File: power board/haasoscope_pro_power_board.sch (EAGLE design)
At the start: 94 parts, among them IC1 TPS5430DDAR, IC10 TPS5430DDAR, IC12 TPS7A7200RGTR, IC2 TPS5430DDAR, IC3 TPS7A7200RGTR, IC4 TPS5430DDAR, IC5 TPS72325DBVR, IC6 TPS5430DDAR, IC7 TPS7A7200RGTR, IC8 TPS5430DDAR, IC9 TPS7A7200RGTR, J1 2p-2.54, J10 2p-2.54, J11 2p-2.54, J13 2p-2.54, J2 2p-2.54, J3 2p-2.54, J4 2p-2.54, J5 2p-2.54, J6 2p-2.54, J7 2p-2.54, J8 2p-2.54, J9 2p-2.54

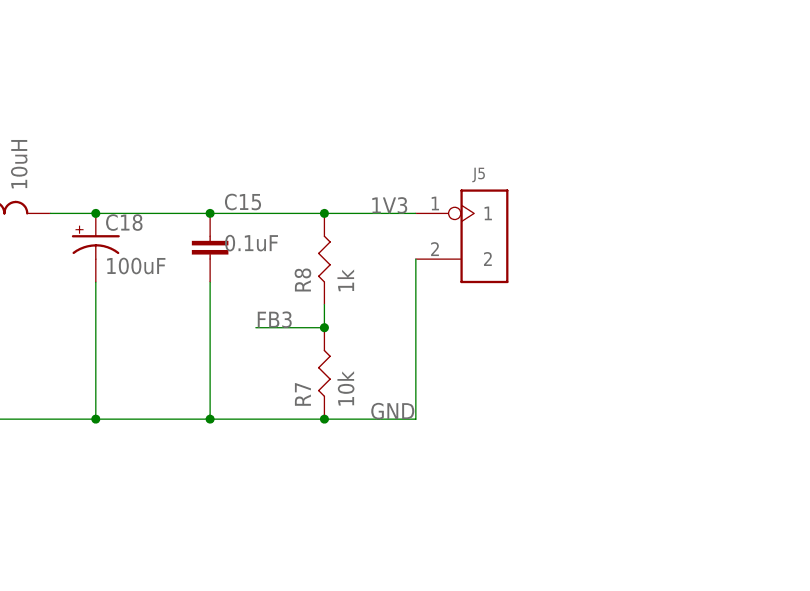
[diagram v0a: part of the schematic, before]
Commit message: 1.3->1.8 V for VLVDS
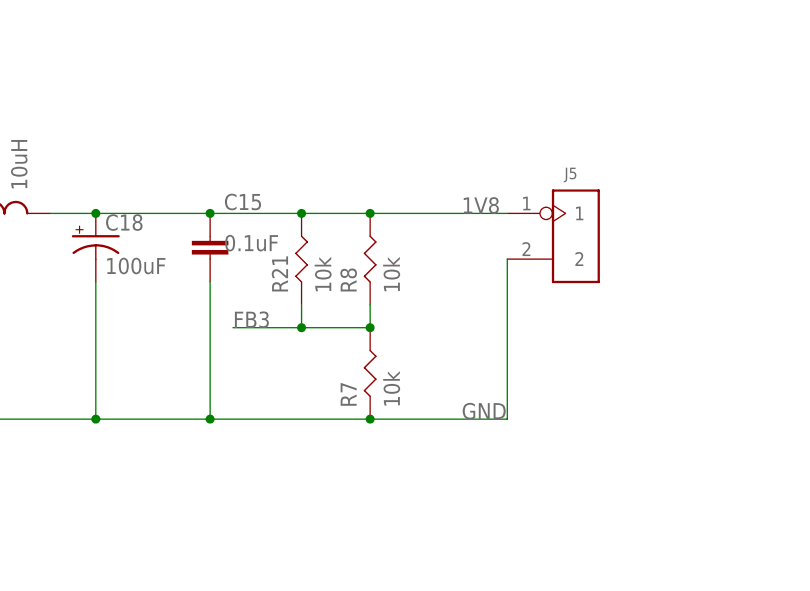
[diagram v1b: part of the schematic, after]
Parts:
- added R21: 10k, FlashPCB_Resistors:RES-0402
- R8: value 1k -> 10k
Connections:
- removed net 1V3: C15.1, C18.+, J5.1, L4.2, R8.P$2
- new net 1V8: C15.1, C18.+, J5.1, L4.2, R21.P$2, R8.P$2
- net FB3: now also R21.P$1
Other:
- note added: "VLVDS ~ 1.8V"
- note added: "Vout = (5k/10k +1) * 1.221 V =1.5*1.221 V = ~ 1.8V"
- note removed: "VLVDS ~ 1.3V"
- note removed: "Vout = (R8/R7 +1) * 1.221 V =1.1*1.221 V = ~ 1.3V"
- moved on the sheet: J5, R7, R8
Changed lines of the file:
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@@
 </part>
 <part name="IC4" library="TPS5430DDAR" deviceset="TPS5430DDAR" device=""/>
-<part name="R8" library="FlashPCB_Resistors" deviceset="RES-0402" device="" value="1k"/>
+<part name="R8" library="FlashPCB_Resistors" deviceset="RES-0402" device="" value="10k"/>
 <part name="L6" library="SparkFun-Passives" deviceset="INDUCTOR" device="PWR" value="10uH">
 <attribute name="LCSC" value="C339970"/>
@@
 <part name="R18" library="FlashPCB_Resistors" deviceset="RES-0402" device="" value="3.3k"/>
 <part name="GND15" library="SparkFun-PowerSymbols" library_urn="urn:adsk.eagle:library:530" deviceset="GND" device=""/>
+<part name="R21" library="FlashPCB_Resistors" deviceset="RES-0402" device="" value="10k"/>
 </parts>
 <sheets>
@@
 <text x="149.86" y="17.78" size="1.778" layer="90">Vout = -(Rtop/Rbot +1) * 1.221 V
 = -2.33*1.221 V = ~ -2.8V</text>
-<text x="137.16" y="124.46" size="1.778" layer="90">Vout = (R8/R7 +1) * 1.221 V
-=1.1*1.221 V = ~ 1.3V</text>
+<text x="137.16" y="124.46" size="1.778" layer="90">Vout = (5k/10k +1) * 1.221 V
+=1.5*1.221 V = ~ 1.8V</text>
 <text x="137.16" y="187.96" size="1.778" layer="90">Vout = (R12/R11 +1) * 1.221 V
 =2*1.221 V = ~ 2.4V</text>
@@
 <text x="137.16" y="325.12" size="1.778" layer="90">Vout = (R20/R19 +1) * 1.221 V
 =3*1.221 V = ~ 3.7V</text>
-<text x="177.8" y="109.22" size="1.778" layer="90">VLVDS ~ 1.3V</text>
+<text x="187.96" y="109.22" size="1.778" layer="90">VLVDS ~ 1.8V</text>
 <text x="177.8" y="48.26" size="1.778" layer="90">V+ for input amp reg ~ 2.8V</text>
 <text x="177.8" y="-5.08" size="1.778" layer="90">V- for input amp reg ~ -2.8V</text>
@@
 <attribute name="LCSC" x="124.46" y="121.92" size="1.778" layer="96" rot="R90" display="off"/>
 </instance>
-<instance part="R7" gate="G$1" x="162.56" y="104.14" smashed="yes" rot="R90">
-<attribute name="NAME" x="161.0614" y="100.33" size="1.778" layer="95" rot="R90"/>
-<attribute name="VALUE" x="165.862" y="100.33" size="1.778" layer="96" rot="R90"/>
+<instance part="R7" gate="G$1" x="167.64" y="104.14" smashed="yes" rot="R90">
+<attribute name="NAME" x="166.1414" y="100.33" size="1.778" layer="95" rot="R90"/>
+<attribute name="VALUE" x="170.942" y="100.33" size="1.778" layer="96" rot="R90"/>
 </instance>
 <instance part="D4" gate="G$1" x="109.22" y="114.3" smashed="yes" rot="R90">
@@
 <attribute name="LCSC" x="109.22" y="114.3" size="1.778" layer="96" rot="R90" display="off"/>
 </instance>
-<instance part="J5" gate="G$1" x="180.34" y="119.38" smashed="yes">
-<attribute name="NAME" x="179.07" y="125.73" size="1.27" layer="95" ratio="10"/>
+<instance part="J5" gate="G$1" x="190.5" y="119.38" smashed="yes">
+<attribute name="NAME" x="189.23" y="125.73" size="1.27" layer="95" ratio="10"/>
 </instance>
 <instance part="C15" gate="C$1" x="149.86" y="119.38" smashed="yes">
@@
 <attribute name="VALUE" x="16.51" y="127" size="1.778" layer="96" align="center-left"/>
 </instance>
-<instance part="R8" gate="G$1" x="162.56" y="116.84" smashed="yes" rot="R90">
-<attribute name="NAME" x="161.0614" y="113.03" size="1.778" layer="95" rot="R90"/>
-<attribute name="VALUE" x="165.862" y="113.03" size="1.778" layer="96" rot="R90"/>
+<instance part="R8" gate="G$1" x="167.64" y="116.84" smashed="yes" rot="R90">
+<attribute name="NAME" x="166.1414" y="113.03" size="1.778" layer="95" rot="R90"/>
+<attribute name="VALUE" x="170.942" y="113.03" size="1.778" layer="96" rot="R90"/>
 </instance>
 <instance part="L6" gate="G$1" x="124.46" y="185.42" smashed="yes" rot="R90">
@@
 <instance part="GND15" gate="1" x="314.96" y="345.44" smashed="yes">
 <attribute name="VALUE" x="314.96" y="345.186" size="1.778" layer="96" align="top-center"/>
+</instance>
+<instance part="R21" gate="G$1" x="160.02" y="116.84" smashed="yes" rot="R90">
+<attribute name="NAME" x="158.5214" y="113.03" size="1.778" layer="95" rot="R90"/>
+<attribute name="VALUE" x="163.322" y="113.03" size="1.778" layer="96" rot="R90"/>
 </instance>
 </instances>
@@
 <segment>
 <pinref part="R7" gate="G$1" pin="P$1"/>
-<wire x1="172.72" y1="99.06" x2="162.56" y2="99.06" width="0.1524" layer="91"/>
+<wire x1="182.88" y1="99.06" x2="167.64" y2="99.06" width="0.1524" layer="91"/>
 <pinref part="D4" gate="G$1" pin="A"/>
 <wire x1="109.22" y1="111.76" x2="109.22" y2="99.06" width="0.1524" layer="91"/>
 <wire x1="109.22" y1="99.06" x2="137.16" y2="99.06" width="0.1524" layer="91"/>
-<junction x="162.56" y="99.06"/>
+<junction x="167.64" y="99.06"/>
 <wire x1="137.16" y1="99.06" x2="149.86" y2="99.06" width="0.1524" layer="91"/>
-<wire x1="149.86" y1="99.06" x2="162.56" y2="99.06" width="0.1524" layer="91"/>
+<wire x1="149.86" y1="99.06" x2="167.64" y2="99.06" width="0.1524" layer="91"/>
 <wire x1="137.16" y1="114.3" x2="137.16" y2="99.06" width="0.1524" layer="91"/>
 <junction x="137.16" y="99.06"/>
 <wire x1="149.86" y1="114.3" x2="149.86" y2="99.06" width="0.1524" layer="91"/>
 <junction x="149.86" y="99.06"/>
-<label x="167.64" y="99.06" size="1.778" layer="95"/>
+<label x="177.8" y="99.06" size="1.778" layer="95"/>
 <pinref part="J5" gate="G$1" pin="2"/>
-<wire x1="172.72" y1="116.84" x2="172.72" y2="99.06" width="0.1524" layer="91"/>
+<wire x1="182.88" y1="116.84" x2="182.88" y2="99.06" width="0.1524" layer="91"/>
 <pinref part="C15" gate="C$1" pin="2"/>
 <pinref part="C18" gate="G$1" pin="-"/>
@@
 </segment>
 <segment>
-<label x="154.94" y="109.22" size="1.778" layer="95"/>
+<label x="152.4" y="109.22" size="1.778" layer="95"/>
 <pinref part="R7" gate="G$1" pin="P$2"/>
-<wire x1="154.94" y1="109.22" x2="162.56" y2="109.22" width="0.1524" layer="91"/>
-<wire x1="162.56" y1="111.76" x2="162.56" y2="109.22" width="0.1524" layer="91"/>
-<junction x="162.56" y="109.22"/>
+<wire x1="152.4" y1="109.22" x2="160.02" y2="109.22" width="0.1524" layer="91"/>
+<wire x1="160.02" y1="109.22" x2="167.64" y2="109.22" width="0.1524" layer="91"/>
+<wire x1="167.64" y1="111.76" x2="167.64" y2="109.22" width="0.1524" layer="91"/>
+<junction x="167.64" y="109.22"/>
 <pinref part="R8" gate="G$1" pin="P$1"/>
-</segment>
-</net>
-<net name="1V3" class="0">
+<pinref part="R21" gate="G$1" pin="P$1"/>
+<wire x1="160.02" y1="111.76" x2="160.02" y2="109.22" width="0.1524" layer="91"/>
+<junction x="160.02" y="109.22"/>
+</segment>
+</net>
+<net name="1V8" class="0">
 <segment>
 <pinref part="L4" gate="G$1" pin="2"/>
 <wire x1="132.08" y1="121.92" x2="137.16" y2="121.92" width="0.1524" layer="91"/>
 <wire x1="137.16" y1="121.92" x2="149.86" y2="121.92" width="0.1524" layer="91"/>
-<wire x1="149.86" y1="121.92" x2="162.56" y2="121.92" width="0.1524" layer="91"/>
-<label x="167.64" y="121.92" size="1.778" layer="95"/>
+<wire x1="149.86" y1="121.92" x2="160.02" y2="121.92" width="0.1524" layer="91"/>
+<label x="177.8" y="121.92" size="1.778" layer="95"/>
 <pinref part="J5" gate="G$1" pin="1"/>
 <pinref part="C15" gate="C$1" pin="1"/>
@@
 <pinref part="C18" gate="G$1" pin="+"/>
 <junction x="137.16" y="121.92"/>
-<wire x1="162.56" y1="121.92" x2="172.72" y2="121.92" width="0.1524" layer="91"/>
+<wire x1="160.02" y1="121.92" x2="167.64" y2="121.92" width="0.1524" layer="91"/>
+<wire x1="167.64" y1="121.92" x2="182.88" y2="121.92" width="0.1524" layer="91"/>
 <pinref part="R8" gate="G$1" pin="P$2"/>
-<junction x="162.56" y="121.92"/>
-</segment>
-</net>
+<junction x="167.64" y="121.92"/>
+<pinref part="R21" gate="G$1" pin="P$2"/>
+<junction x="160.02" y="121.92"/>
+</segment>
+</net>

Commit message: add 2.5D for fpga, and add 1V9D for VLVDS
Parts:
- added C28, C38: 10uF, Nordic_nRF:CAPACITOR_0805_N
- added C29, C43: 0.1uF, Nordic_nRF:CAPACITOR_0402_N
- added IC11, IC14: TPS7A7200RGTR, TPS7A7200RGTR:TPS7A7200RGTR
- added J12, J15: 2p-2.54, Seeed-Connector:DIP-BLACK-MALE-HEADER-VERT(2P-2.54)
- added R22, R24: 20k, FlashPCB_Resistors:RES-0402
- R8: value 10k -> 3.3k
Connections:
- removed net 1V8: C15.1, C18.+, J5.1, L4.2, R21.P$2, R8.P$2
- new net 1V9DOUT: C28.1, C29.1, IC11.OUT_1, IC11.OUT_2, IC11.SNS, J12.2, R22.P$1
- new net 2V5DOUT: C38.1, C43.1, IC14.OUT_1, IC14.OUT_2, IC14.SNS, J15.2, R24.P$1
- new net 2V8D: C15.1, C18.+, IC14.EN, IC14.IN_1, IC14.IN_2, J5.1, L4.2, R8.P$2
- new net N$7: R21.P$2, R8.P$1
- new net PG1V9D: IC11.PG, R22.P$2
- new net PG2V5D: IC14.PG, R24.P$2
- net 2V4: now also IC11.EN, IC11.IN_1, IC11.IN_2
- net FB3: no longer R8.P$1
- net GND: now also C28.2, C29.2, C38.2, C43.2, IC11.200MV, IC11.400MV, IC11.800MV, IC11.EP, IC11.GND, IC14.1.6V, IC14.400MV, IC14.800MV, IC14.EP, IC14.GND, J12.1, J15.1
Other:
- note added: "V+ for 2v5D reg ~ 2.8V"
- note added: "VLVDS = 1.9V"
- note removed: "VLVDS ~ 1.8V"
- note removed: "Vout = (5k/10k +1) * 1.221 V =1.5*1.221 V = ~ 1.8V"
- moved on the sheet: C1, C10, C13, C14, C2, C27, C3, C30, C35, C4, C5, C6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

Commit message: power connector etc
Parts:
- added J14: 8pin, SparkFun-Connectors:CONN_08"
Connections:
- net 1V1OUT: now also J14.4
- net 1V9DOUT: now also J14.6
- net 1V9OUT: now also J14.5
- net 2V5DOUT: now also J14.8
- net 3V3OUT: now also J14.1
- net GND: now also J14.2, J14.3, J14.7
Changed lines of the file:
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@@
 <part name="C43" library="Nordic_nRF" library_urn="urn:adsk.eagle:library:169009" deviceset="CAPACITOR" device="_0402_N" package3d_urn="urn:adsk.eagle:package:2593732/1" value="0.1uF"/>
 <part name="GND17" library="SparkFun-PowerSymbols" library_urn="urn:adsk.eagle:library:530" deviceset="GND" device=""/>
+<part name="J14" library="SparkFun-Connectors" library_urn="urn:adsk.eagle:library:513" deviceset="CONN_08" device="&quot;" package3d_urn="urn:adsk.eagle:package:38138/1" value="8pin"/>
 </parts>
 <sheets>
@@
 <attribute name="VALUE" x="279.4" y="129.286" size="1.778" layer="96" align="top-center"/>
 </instance>
+<instance part="J14" gate="G$1" x="365.76" y="2.54" smashed="yes" rot="R180"/>
 </instances>
 <busses>
@@
 <junction x="264.16" y="81.28"/>
 </segment>
+<segment>
+<wire x1="360.68" y1="7.62" x2="353.06" y2="7.62" width="0.1524" layer="91"/>
+<pinref part="J14" gate="G$1" pin="2"/>
+<label x="353.06" y="7.62" size="1.778" layer="95"/>
+</segment>
+<segment>
+<pinref part="J14" gate="G$1" pin="7"/>
+<wire x1="360.68" y1="-5.08" x2="353.06" y2="-5.08" width="0.1524" layer="91"/>
+<label x="353.06" y="-5.08" size="1.778" layer="95"/>
+</segment>
+<segment>
+<wire x1="360.68" y1="5.08" x2="353.06" y2="5.08" width="0.1524" layer="91"/>
+<pinref part="J14" gate="G$1" pin="3"/>
+<label x="353.06" y="5.08" size="1.778" layer="95"/>
+</segment>
 </net>
 <net name="SW1" class="0">
@@
 <label x="236.22" y="317.5" size="1.778" layer="95"/>
 </segment>
+<segment>
+<wire x1="360.68" y1="10.16" x2="353.06" y2="10.16" width="0.1524" layer="91"/>
+<label x="353.06" y="10.16" size="1.778" layer="95"/>
+<pinref part="J14" gate="G$1" pin="1"/>
+</segment>
 </net>
 <net name="PG3V3" class="0">
@@
 <label x="236.22" y="180.34" size="1.778" layer="95"/>
 </segment>
+<segment>
+<pinref part="J14" gate="G$1" pin="5"/>
+<wire x1="360.68" y1="0" x2="353.06" y2="0" width="0.1524" layer="91"/>
+<label x="350.52" y="0" size="1.778" layer="95"/>
+</segment>
 </net>
 <net name="PG1V9" class="0">
@@
 <label x="236.22" y="248.92" size="1.778" layer="95"/>
 </segment>
+<segment>
+<pinref part="J14" gate="G$1" pin="4"/>
+<wire x1="360.68" y1="2.54" x2="353.06" y2="2.54" width="0.1524" layer="91"/>
+<label x="350.52" y="2.54" size="1.778" layer="95"/>
+</segment>
 </net>
 <net name="PG1V1" class="0">
@@
 <junction x="365.76" y="213.36"/>
 </segment>
+<segment>
+<pinref part="J14" gate="G$1" pin="6"/>
+<wire x1="360.68" y1="-2.54" x2="353.06" y2="-2.54" width="0.1524" layer="91"/>
+<label x="350.52" y="-2.54" size="1.778" layer="95"/>
+</segment>
 </net>
 <net name="N$7" class="0">
@@
 <label x="236.22" y="106.68" size="1.778" layer="95"/>
 </segment>
-</net>
+<segment>
+<pinref part="J14" gate="G$1" pin="8"/>
+<wire x1="360.68" y1="-7.62" x2="353.06" y2="-7.62" width="0.1524" layer="91"/>
+<label x="353.06" y="-7.62" size="1.778" layer="95"/>
+</segment>
+</net>

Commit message: power connector etc
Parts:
- renumbered J14 to J16
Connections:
- net 1V1OUT: now also J16.2; no longer J16.4
- net 1V9DOUT: now also J16.4; no longer J16.6
- net 1V9OUT: now also J16.3; no longer J16.5
- net 2V5-: now also J16.8
- net 2V5DOUT: now also J16.6; no longer J16.8
- net 2V5OUT: now also J16.7
- net GND: now also J16.5; no longer J16.2, J16.3, J16.7
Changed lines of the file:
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@@
 <part name="C43" library="Nordic_nRF" library_urn="urn:adsk.eagle:library:169009" deviceset="CAPACITOR" device="_0402_N" package3d_urn="urn:adsk.eagle:package:2593732/1" value="0.1uF"/>
 <part name="GND17" library="SparkFun-PowerSymbols" library_urn="urn:adsk.eagle:library:530" deviceset="GND" device=""/>
-<part name="J14" library="SparkFun-Connectors" library_urn="urn:adsk.eagle:library:513" deviceset="CONN_08" device="&quot;" package3d_urn="urn:adsk.eagle:package:38138/1" value="8pin"/>
+<part name="J16" library="SparkFun-Connectors" library_urn="urn:adsk.eagle:library:513" deviceset="CONN_08" device="&quot;" package3d_urn="urn:adsk.eagle:package:38138/1" value="8pin"/>
 </parts>
 <sheets>
@@
 <attribute name="VALUE" x="279.4" y="129.286" size="1.778" layer="96" align="top-center"/>
 </instance>
-<instance part="J14" gate="G$1" x="365.76" y="2.54" smashed="yes" rot="R180"/>
+<instance part="J16" gate="G$1" x="365.76" y="2.54" smashed="yes" rot="R180"/>
 </instances>
 <busses>
@@
 </segment>
 <segment>
-<wire x1="360.68" y1="7.62" x2="353.06" y2="7.62" width="0.1524" layer="91"/>
-<pinref part="J14" gate="G$1" pin="2"/>
-<label x="353.06" y="7.62" size="1.778" layer="95"/>
-</segment>
-<segment>
-<pinref part="J14" gate="G$1" pin="7"/>
-<wire x1="360.68" y1="-5.08" x2="353.06" y2="-5.08" width="0.1524" layer="91"/>
-<label x="353.06" y="-5.08" size="1.778" layer="95"/>
-</segment>
-<segment>
-<wire x1="360.68" y1="5.08" x2="353.06" y2="5.08" width="0.1524" layer="91"/>
-<pinref part="J14" gate="G$1" pin="3"/>
-<label x="353.06" y="5.08" size="1.778" layer="95"/>
+<wire x1="360.68" y1="0" x2="353.06" y2="0" width="0.1524" layer="91"/>
+<label x="353.06" y="0" size="1.778" layer="95"/>
+<pinref part="J16" gate="G$1" pin="5"/>
 </segment>
 </net>
@@
 </segment>
 <segment>
-<wire x1="360.68" y1="10.16" x2="353.06" y2="10.16" width="0.1524" layer="91"/>
-<label x="353.06" y="10.16" size="1.778" layer="95"/>
-<pinref part="J14" gate="G$1" pin="1"/>
+<wire x1="360.68" y1="10.16" x2="350.52" y2="10.16" width="0.1524" layer="91"/>
+<label x="350.52" y="10.16" size="1.778" layer="95"/>
+<pinref part="J16" gate="G$1" pin="1"/>
 </segment>
 </net>
@@
 </segment>
 <segment>
-<pinref part="J14" gate="G$1" pin="5"/>
-<wire x1="360.68" y1="0" x2="353.06" y2="0" width="0.1524" layer="91"/>
-<label x="350.52" y="0" size="1.778" layer="95"/>
+<wire x1="360.68" y1="5.08" x2="353.06" y2="5.08" width="0.1524" layer="91"/>
+<label x="350.52" y="5.08" size="1.778" layer="95"/>
+<pinref part="J16" gate="G$1" pin="3"/>
 </segment>
 </net>
@@
 </segment>
 <segment>
-<pinref part="J14" gate="G$1" pin="4"/>
-<wire x1="360.68" y1="2.54" x2="353.06" y2="2.54" width="0.1524" layer="91"/>
-<label x="350.52" y="2.54" size="1.778" layer="95"/>
+<wire x1="360.68" y1="7.62" x2="353.06" y2="7.62" width="0.1524" layer="91"/>
+<label x="350.52" y="7.62" size="1.778" layer="95"/>
+<pinref part="J16" gate="G$1" pin="2"/>
 </segment>
 </net>
@@
 <wire x1="279.4" y1="-43.18" x2="274.32" y2="-43.18" width="0.1524" layer="91"/>
 <label x="274.32" y="-43.18" size="1.778" layer="95"/>
+</segment>
+<segment>
+<pinref part="J16" gate="G$1" pin="8"/>
+<wire x1="360.68" y1="-7.62" x2="350.52" y2="-7.62" width="0.1524" layer="91"/>
+<label x="350.52" y="-7.62" size="1.778" layer="95"/>
 </segment>
 </net>
@@
 <label x="236.22" y="22.86" size="1.778" layer="95"/>
 </segment>
+<segment>
+<pinref part="J16" gate="G$1" pin="7"/>
+<wire x1="360.68" y1="-5.08" x2="353.06" y2="-5.08" width="0.1524" layer="91"/>
+<label x="350.52" y="-5.08" size="1.778" layer="95"/>
+</segment>
 </net>
 <net name="PG25" class="0">
@@
 </segment>
 <segment>
-<pinref part="J14" gate="G$1" pin="6"/>
-<wire x1="360.68" y1="-2.54" x2="353.06" y2="-2.54" width="0.1524" layer="91"/>
-<label x="350.52" y="-2.54" size="1.778" layer="95"/>
+<wire x1="360.68" y1="2.54" x2="353.06" y2="2.54" width="0.1524" layer="91"/>
+<label x="350.52" y="2.54" size="1.778" layer="95"/>
+<pinref part="J16" gate="G$1" pin="4"/>
 </segment>
 </net>
@@
 </segment>
 <segment>
-<pinref part="J14" gate="G$1" pin="8"/>
-<wire x1="360.68" y1="-7.62" x2="353.06" y2="-7.62" width="0.1524" layer="91"/>
-<label x="353.06" y="-7.62" size="1.778" layer="95"/>
-</segment>
-</net>
+<wire x1="360.68" y1="-2.54" x2="350.52" y2="-2.54" width="0.1524" layer="91"/>
+<label x="350.52" y="-2.54" size="1.778" layer="95"/>
+<pinref part="J16" gate="G$1" pin="6"/>
+</segment>
+</net>

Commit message: Power board v1.11 with +0.1V options, 2v5, etc.
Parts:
- added CN1: 12Vin, adafruit:DCBARRELPTH
- added J17, J18, J19: 2p-2.54, Seeed-Connector:DIP-BLACK-MALE-HEADER-VERT(2P-2.54)
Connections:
- new net N$10: IC7.100MV, J17.2
- new net N$8: IC3.100MV, J19.2
- new net N$9: IC9.100MV, J18.2
- net GND: now also CN1.GND, CN1.GNDBREAK, J17.1, J18.1, J19.1; no longer IC14.800MV
- net VIN: now also CN1.PWR
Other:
- note added: "1V1"
- note added: "1V9"
- note added: "2V5+"
- note added: "2V5-"
- note added: "3V3"
- note added: "VFPGA25 = 2.5V"
- moved on the sheet: C10, C3, D3, J3, R14
